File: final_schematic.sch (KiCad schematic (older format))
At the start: 50 parts, among them J1 Conn_Male, J2 Conn_Male, J3 Conn_01x04_Male, J4 Conn_01x02_Male, J5 Conn_Male, J6 Conn_Coaxial, J7 Conn_ARM_JTAG_SWD_10, J8 Conn_Male, SW1 SW_Push, SW2 SW_Push, SW3 SW_Push, U1 BNO055, U2 MTK3339, U3 STM32L476VGTx, U4 RFM95W-868S2, X1 SMA_EDGE_UFL

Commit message: pls no more
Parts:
- C11, C12, C13, C14, C15, C16: value 0.1 uF -> 0.1uF
- C6: value 100nF -> 0.1uF
- C7: value .12uF -> 0.12uF
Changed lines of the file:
@@
 P 2550 2250
 F 0 "C6" H 2665 2296 50  0000 L CNN
-F 1 "100nF" H 2665 2205 50  0000 L CNN
+F 1 "0.1uF" H 2665 2205 50  0000 L CNN
 F 2 "" H 2588 2100 50  0001 C CNN
 F 3 "~" H 2550 2250 50  0001 C CNN
@@
 AR Path="/5F8951F4" Ref="C11"  Part="1"
 F 0 "C11" H 4215 2096 50  0000 L CNN
-F 1 "0.1 uF" H 4215 2005 50  0000 L CNN
+F 1 "0.1uF" H 4215 2005 50  0000 L CNN
 F 2 "" H 4138 1900 50  0001 C CNN
 F 3 "~" H 4100 2050 50  0001 C CNN
@@
 AR Path="/5F8F3A53" Ref="C12"  Part="1"
 F 0 "C12" H 9665 5946 50  0000 L CNN
-F 1 "0.1 uF" H 9665 5855 50  0000 L CNN
+F 1 "0.1uF" H 9665 5855 50  0000 L CNN
 F 2 "" H 9588 5750 50  0001 C CNN
 F 3 "~" H 9550 5900 50  0001 C CNN
@@
 AR Path="/5F8F3A5A" Ref="C13"  Part="1"
 F 0 "C13" H 9915 5946 50  0000 L CNN
-F 1 "0.1 uF" H 9915 5855 50  0000 L CNN
+F 1 "0.1uF" H 9915 5855 50  0000 L CNN
 F 2 "" H 9838 5750 50  0001 C CNN
 F 3 "~" H 9800 5900 50  0001 C CNN
@@
 AR Path="/5F8F3A61" Ref="C14"  Part="1"
 F 0 "C14" H 10165 5946 50  0000 L CNN
-F 1 "0.1 uF" H 10165 5855 50  0000 L CNN
+F 1 "0.1uF" H 10165 5855 50  0000 L CNN
 F 2 "" H 10088 5750 50  0001 C CNN
 F 3 "~" H 10050 5900 50  0001 C CNN
@@
 AR Path="/5F8F3A68" Ref="C15"  Part="1"
 F 0 "C15" H 10415 5946 50  0000 L CNN
-F 1 "0.1 uF" H 10415 5855 50  0000 L CNN
+F 1 "0.1uF" H 10415 5855 50  0000 L CNN
 F 2 "" H 10338 5750 50  0001 C CNN
 F 3 "~" H 10300 5900 50  0001 C CNN
@@
 AR Path="/5F8F3A6F" Ref="C16"  Part="1"
 F 0 "C16" H 10665 5946 50  0000 L CNN
-F 1 "0.1 uF" H 10665 5855 50  0000 L CNN
+F 1 "0.1uF" H 10665 5855 50  0000 L CNN
 F 2 "" H 10588 5750 50  0001 C CNN
 F 3 "~" H 10550 5900 50  0001 C CNN
@@
 P 2850 1100
 F 0 "C7" H 2965 1146 50  0000 L CNN
-F 1 ".12uF" H 2965 1055 50  0000 L CNN
+F 1 "0.12uF" H 2965 1055 50  0000 L CNN
 F 2 "" H 2888 950 50  0001 C CNN
 F 3 "~" H 2850 1100 50  0001 C CNN

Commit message: Footprint Assignments Completed
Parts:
- C1, C11, C12, C5, C6: footprint (none) -> Capacitor_SMD:C_0402_1005Metric_Pad0.74x0.62mm_HandSolder
- C10, C2, C3, C4, C7, C8, C9: footprint (none) -> Capacitor_SMD:C_0603_1608Metric_Pad1.08x0.95mm_HandSolder
- C13: renamed from C18; footprint (none) -> Capacitor_SMD:C_0603_1608Metric_Pad1.08x0.95mm_HandSolder
- C14: renamed from C13; footprint (none) -> Capacitor_SMD:C_0402_1005Metric_Pad0.74x0.62mm_HandSolder
- C15: renamed from C14; footprint (none) -> Capacitor_SMD:C_0402_1005Metric_Pad0.74x0.62mm_HandSolder
- C16: renamed from C15; footprint (none) -> Capacitor_SMD:C_0402_1005Metric_Pad0.74x0.62mm_HandSolder
- C17: renamed from C16; footprint (none) -> Capacitor_SMD:C_0402_1005Metric_Pad0.74x0.62mm_HandSolder
- C18: renamed from C17; footprint (none) -> Capacitor_SMD:C_0402_1005Metric_Pad0.74x0.62mm_HandSolder
- D1: value LED -> LED_HEARTBEAT_R1; footprint (none) -> Diode_SMD:D_0603_1608Metric_Pad1.05x0.95mm_HandSolder
- D2: value LED -> LED_TRANSMIT_G1; footprint (none) -> Diode_SMD:D_0201_0603Metric_Pad0.64x0.40mm_HandSolder
- J1: footprint (none) -> Connector_PinHeader_1.00mm:PinHeader_1x06_P1.00mm_Vertical
- J2, J5: footprint (none) -> Connector_PinHeader_1.00mm:PinHeader_1x01_P1.00mm_Vertical
- J3: footprint (none) -> Connector_PinHeader_1.00mm:PinHeader_1x04_P1.00mm_Vertical
- J4: footprint (none) -> Connector_PinHeader_1.00mm:PinHeader_1x02_P1.00mm_Vertical
- J6, X1: footprint (none) -> Connector_Coaxial:U.FL_Molex_MCRF_73412-0110_Vertical
- J7: renamed from J8; footprint (none) -> Connector_PinHeader_1.00mm:PinHeader_1x01_P1.00mm_Vertical
- R1: footprint (none) -> Resistor_SMD:R_0402_1005Metric_Pad0.72x0.64mm_HandSolder
- R10, R2, R3, R4, R5, R6, R7, R8, R9, Re1, Rf1: footprint (none) -> Resistor_SMD:R_0603_1608Metric_Pad0.98x0.95mm_HandSolder
- RED1: value LED -> LED_GPS_R; footprint (none) -> Diode_SMD:D_0603_1608Metric_Pad1.05x0.95mm_HandSolder
- S1: footprint (none) -> Button_Switch_SMD:SW_DIP_SPSTx01_Slide_Omron_A6S-110x_W8.9mm_P2.54mm
- SW1: value SW_Push -> SW_Push_RST; footprint (none) -> Button_Switch_SMD:SW_SPST_PTS645
- SW2: value SW_Push -> SW_Push_RADIO; footprint (none) -> Button_Switch_SMD:SW_SPST_PTS645
- SW3: value SW_Push -> SW_Push_SESS; footprint (none) -> Button_Switch_SMD:SW_SPST_PTS645
- U2: footprint (none) -> footprint_lib:FGPMMOPA6H
- U4: footprint (none) -> RF_Module:HOPERF_RFM9XW_SMD
- renumbered J7 to J8

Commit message: Grouped Circuits/Re-arranged Schematic
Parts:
- removed C5: 0.1uF, Capacitor_SMD:C_0402_1005Metric_Pad0.74x0.62mm_HandSolder, symbol Device:C
- removed C7: 0.12uF, Capacitor_SMD:C_0603_1608Metric_Pad1.08x0.95mm_HandSolder, symbol Device:C
- removed C9: 0.0068uF, Capacitor_SMD:C_0603_1608Metric_Pad1.08x0.95mm_HandSolder, symbol Device:C
- added C?: 0.1uF, Capacitor_SMD:C_0402_1005Metric_Pad0.74x0.62mm_HandSolder, symbol Device:C
- added C?: 0.12uF, Capacitor_SMD:C_0603_1608Metric_Pad1.08x0.95mm_HandSolder, symbol Device:C
- added C?: 0.0068uF, Capacitor_SMD:C_0603_1608Metric_Pad1.08x0.95mm_HandSolder, symbol Device:C
- R1, Re1, Rf1: symbol Device:R -> Device:R_US
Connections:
- wire segments 243 -> 205
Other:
- note added: "Battery Babysitter \nConnector"
- note added: "GPS"
- note added: "IMU"
- note added: "OLED Breakout \nConnector"
- note added: "Power Switch"
- note added: "Power/Radio Transmit Indicator"
- note added: "STM32L4 Microcontroller"
- note removed: "Battery Babysitter Connector"
- note removed: "GPS\n"
- note removed: "IMU(BNO-005)"
- moved on the sheet: C1, C10, C11, C12, C13, C14, C15, C16, C17, C18, C2, C3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

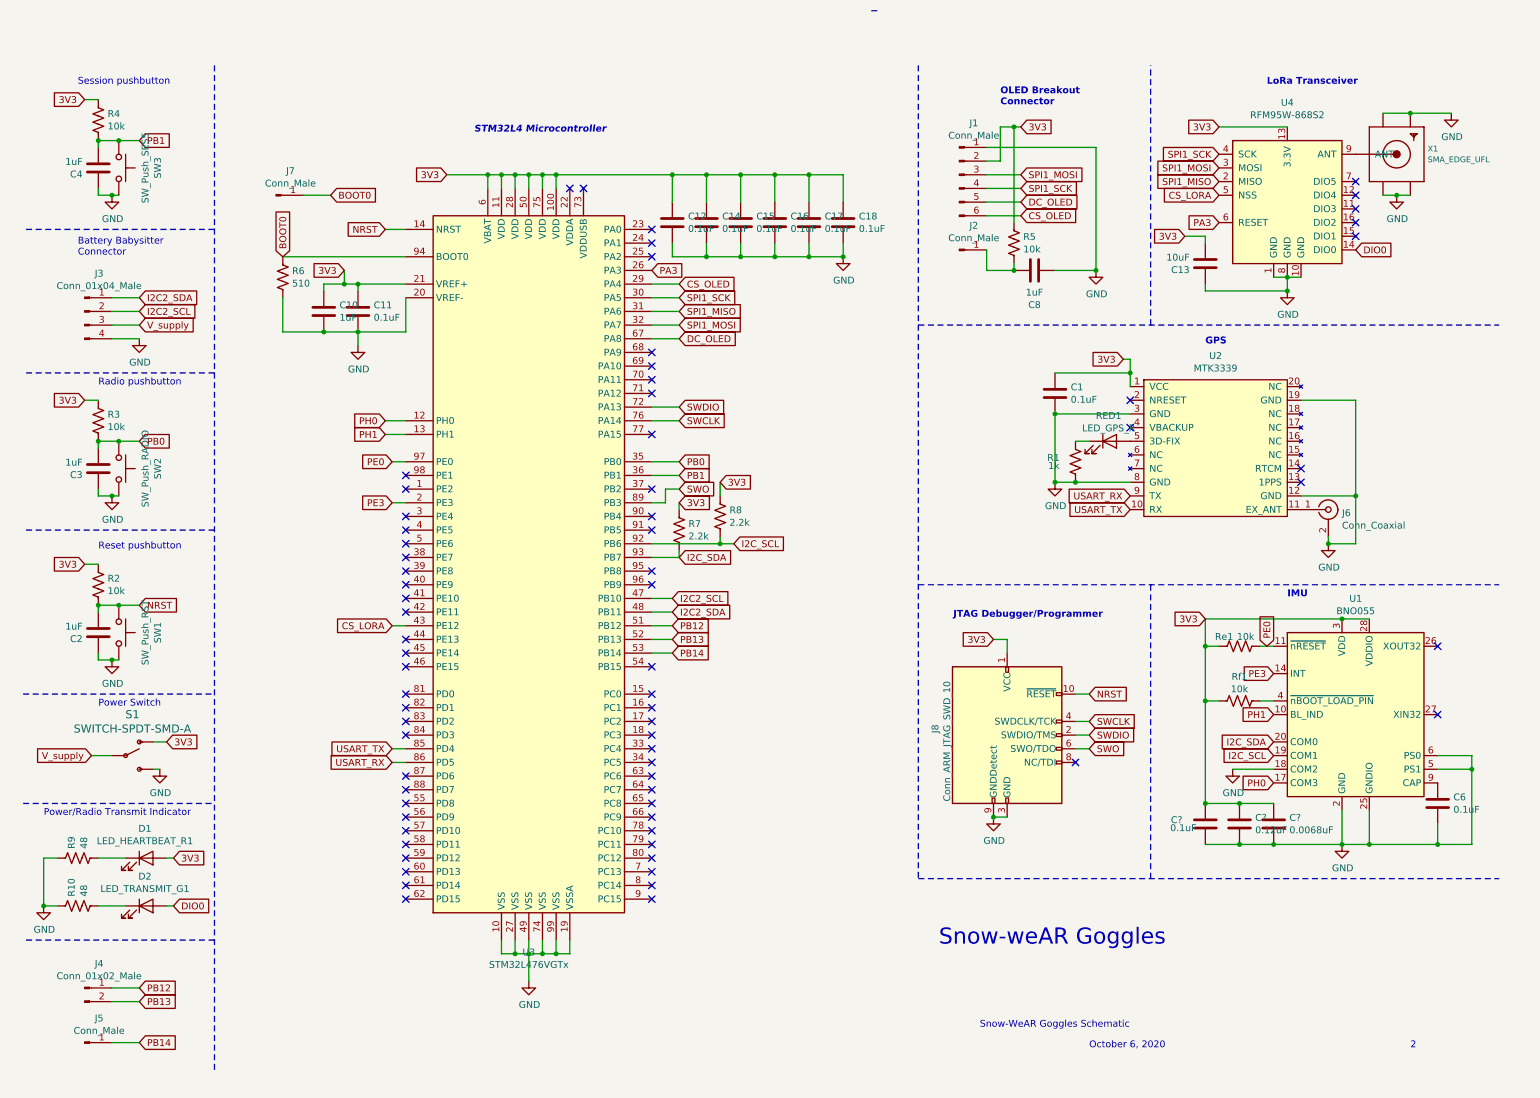
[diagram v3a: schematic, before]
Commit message: Updated Schematic from K improvements, also renamed
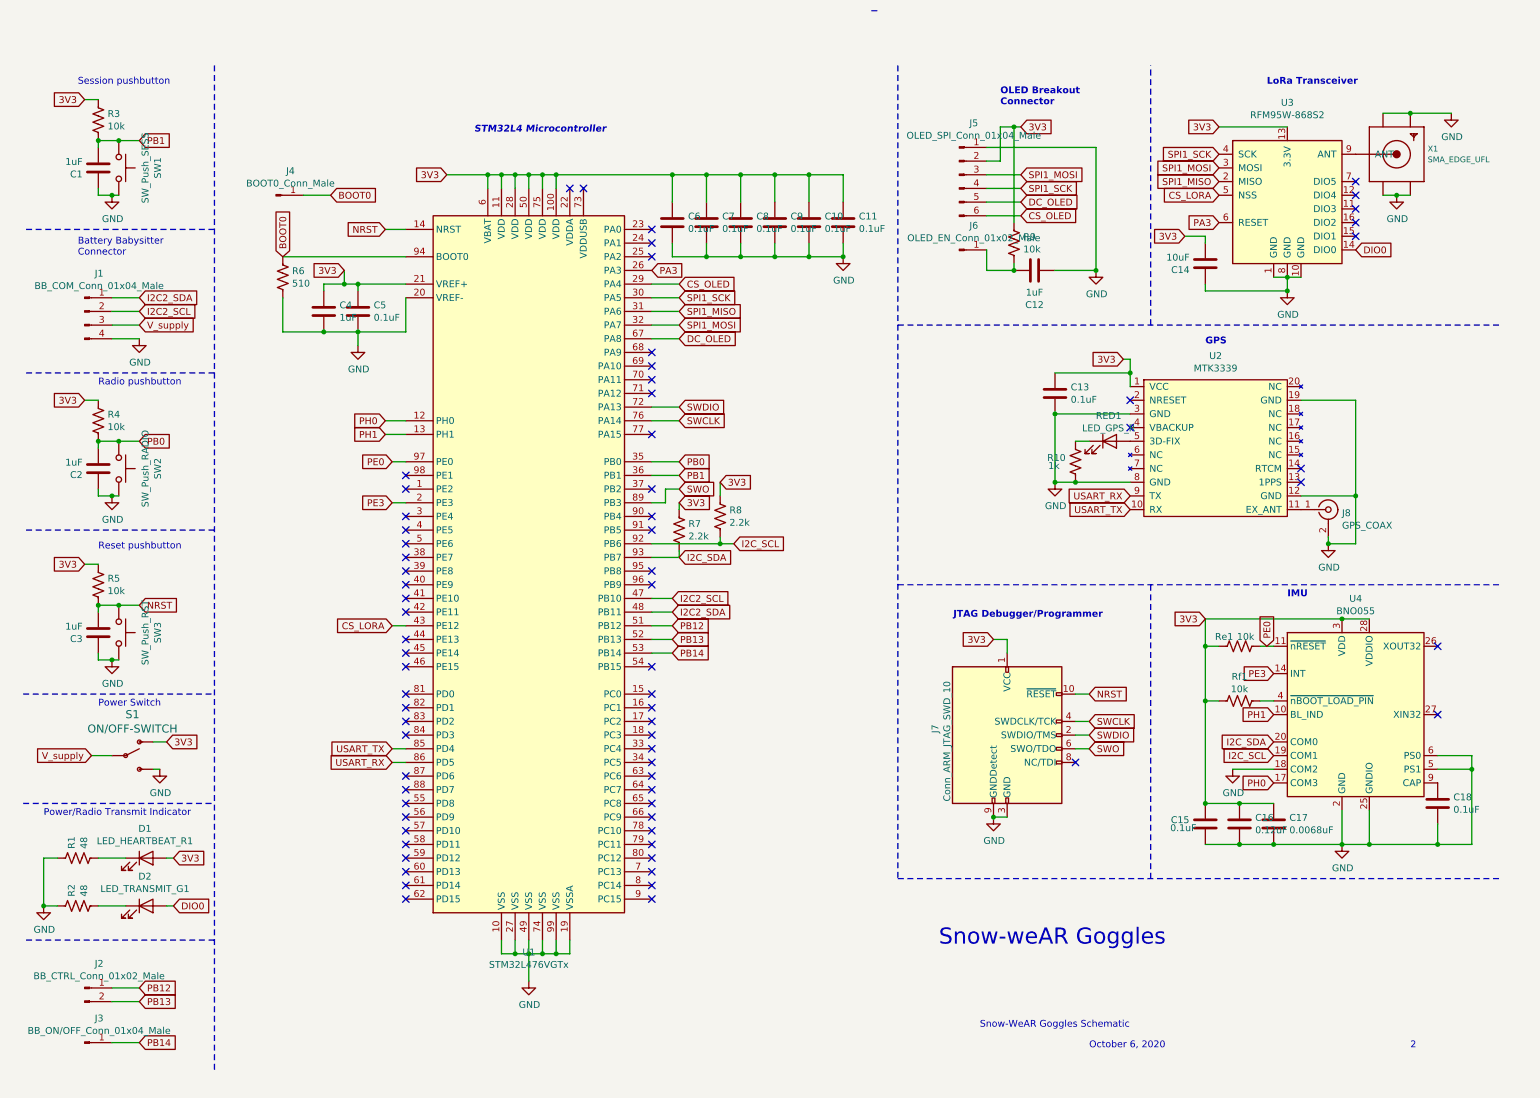
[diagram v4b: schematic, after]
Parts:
- J1: renamed from J3; value Conn_01x04_Male -> BB_COM_Conn_01x04_Male
- J2: renamed from J4; value Conn_01x02_Male -> BB_CTRL_Conn_01x02_Male
- J3: renamed from J5; value Conn_Male -> BB_ON/OFF_Conn_01x04_Male
- J4: renamed from J7; value Conn_Male -> BOOT0_Conn_Male
- J5: renamed from J1; value Conn_Male -> OLED_SPI_Conn_01x04_Male
- J6: renamed from J2; value Conn_Male -> OLED_EN_Conn_01x02_Male
- J8: renamed from J6; value Conn_Coaxial -> GPS_COAX
- S1: value SWITCH-SPDT-SMD-A -> ON/OFF-SWITCH
- gave numbers to parts that had none: 3
- renumbered C4 to C1, C17 to C10, C18 to C11, C8 to C12, C1 to C13, C13 to C14, C6 to C18, C3 to C2, C2 to C3, C10 to C4, C11 to C5, C12 to C6, C14 to C7, C15 to C8, C16 to C9, J8 to J7, R9 to R1, R1 to R10, R10 to R2, R4 to R3, R3 to R4, R2 to R5, R5 to R9, SW3 to SW1, SW1 to SW3, U3 to U1, U4 to U3, U1 to U4

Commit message: all footprints added to .kicad_pcb
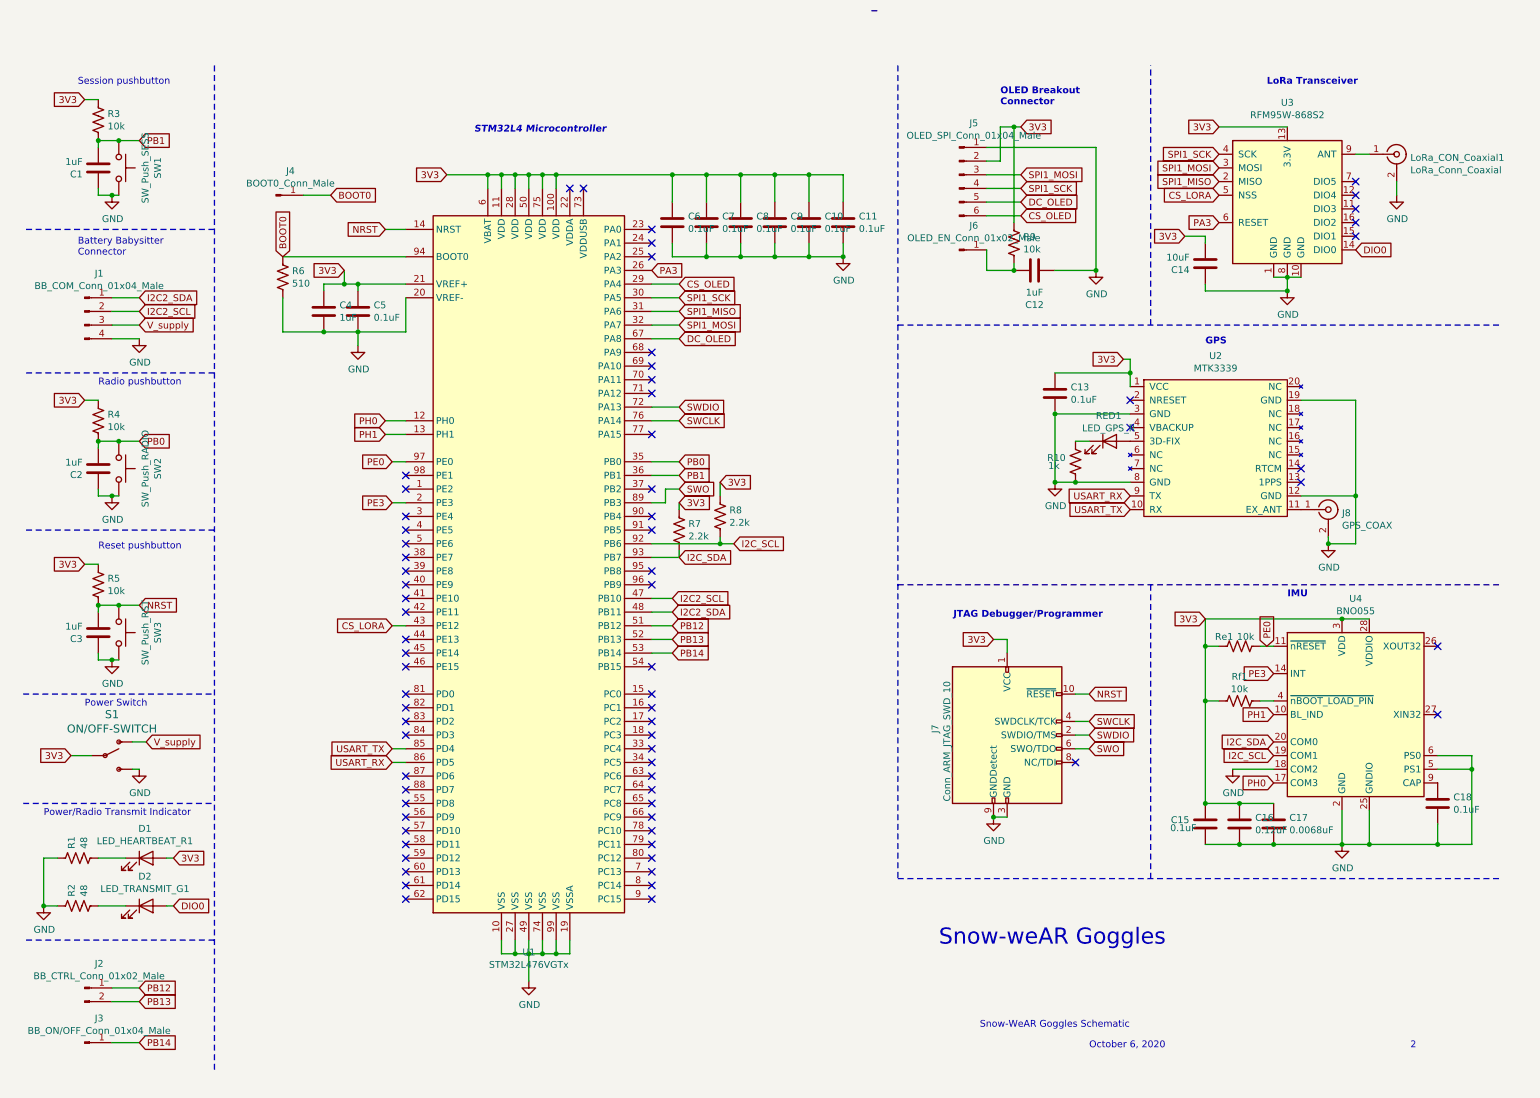
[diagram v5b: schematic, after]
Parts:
- removed X1: SMA_EDGE_UFL, Connector_Coaxial:U.FL_Molex_MCRF_73412-0110_Vertical, symbol final_schematic-eagle-import:SMACONNECTOR_EDGE_UFL
- added LoRa_CON_Coaxial1: LoRa_Conn_Coaxial, Connector_Coaxial:U.FL_Molex_MCRF_73412-0110_Vertical, symbol Connector:Conn_Coaxial
- S1: footprint Button_Switch_SMD:SW_DIP_SPSTx01_Slide_Omron_A6S-110x_W8.9mm_P2.54mm -> Button_Switch_SMD:SW_SP3T_PCM13
- SW1: footprint Button_Switch_SMD:SW_SPST_PTS645 -> Button_Switch_SMD:SW_SPDT_CK-JS102011SAQN
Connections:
- net 3V3: now also S1.2 (P); no longer S1.1 (O)
- net GND: now also LoRa_CON_Coaxial1.2 (Ext)
- net V_supply: now also S1.1 (O); no longer S1.2 (P)
- net at U3.9 (ANT): now also LoRa_CON_Coaxial1.1 (In)
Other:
- moved on the sheet: S1
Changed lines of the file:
@@
 Text GLabel 9200 1100 0    50   Input ~ 0
 SPI1_SCK
-$Comp
-L final_schematic-eagle-import:SMACONNECTOR_EDGE_UFL X1
-U 1 1 5F7841CC
-P 10500 1100
-F 0 "X1" H 10727 1140 42  0000 L CNN
-F 1 "SMA_EDGE_UFL" H 10727 1061 42  0000 L CNN
-F 2 "Connector_Coaxial:U.FL_Molex_MCRF_73412-0110_Vertical" H 10500 1100 50  0001 C CNN
-F 3 "" H 10500 1100 50  0001 C CNN
-	1    10500 1100
-	1    0    0    -1
-$EndComp
-Wire Wire Line
-	10400 1400 10500 1400
-$Comp
-L power:GND #PWR018
-U 1 1 5F7A7227
-P 10900 800
-F 0 "#PWR018" H 10900 550 50  0001 C CNN
-F 1 "GND" H 10905 627 50  0000 C CNN
-F 2 "" H 10900 800 50  0001 C CNN
-F 3 "" H 10900 800 50  0001 C CNN
-	1    10900 800
-	1    0    0    -1
-$EndComp
 Text GLabel 9200 1300 0    50   Input ~ 0
 SPI1_MISO
@@
 L final_schematic-rescue:SWITCH-SPDT-SMD-A-schematic-eagle-import S1
 U 1 1 60374331
-P 1200 5500
-F 0 "S1" H 1250 5801 59  0000 C CNN
-F 1 "ON/OFF-SWITCH" H 1250 5696 59  0000 C CNN
-F 2 "Button_Switch_SMD:SW_DIP_SPSTx01_Slide_Omron_A6S-110x_W8.9mm_P2.54mm" H 1200 5500 50  0001 C CNN
-F 3 "" H 1200 5500 50  0001 C CNN
-	1    1200 5500
+P 1050 5500
+F 0 "S1" H 1100 5801 59  0000 C CNN
+F 1 "ON/OFF-SWITCH" H 1100 5696 59  0000 C CNN
+F 2 "Button_Switch_SMD:SW_SP3T_PCM13" H 1050 5500 50  0001 C CNN
+F 3 "" H 1050 5500 50  0001 C CNN
+	1    1050 5500
 	1    0    0    -1
 $EndComp
@@
 L power:GND #PWR06
 U 1 1 6038CE54
-P 1450 5600
-F 0 "#PWR06" H 1450 5350 50  0001 C CNN
-F 1 "GND" H 1455 5427 50  0000 C CNN
-F 2 "" H 1450 5600 50  0001 C CNN
-F 3 "" H 1450 5600 50  0001 C CNN
-	1    1450 5600
-	1    0    0    -1
-$EndComp
-Text GLabel 950  5500 0    50   Input ~ 0
+P 1300 5600
+F 0 "#PWR06" H 1300 5350 50  0001 C CNN
+F 1 "GND" H 1305 5427 50  0000 C CNN
+F 2 "" H 1300 5600 50  0001 C CNN
+F 3 "" H 1300 5600 50  0001 C CNN
+	1    1300 5600
+	1    0    0    -1
+$EndComp
+Text GLabel 1350 5400 2    50   Input ~ 0
 V_supply
-Text GLabel 1500 5400 2    50   Input ~ 0
+Text GLabel 800  5500 0    50   Input ~ 0
 3V3
 Wire Wire Line
-	950  5500 1100 5500
-Wire Wire Line
-	1400 5400 1500 5400
-Wire Wire Line
-	1450 5600 1400 5600
+	800  5500 950  5500
+Wire Wire Line
+	1250 5400 1350 5400
+Wire Wire Line
+	1300 5600 1250 5600
 $Comp
 L Switch:SW_Push SW3
@@
 F 0 "SW1" H 1150 1485 50  0000 C CNN
 F 1 "SW_Push_SESS" H 1150 1394 50  0000 C CNN
-F 2 "Button_Switch_SMD:SW_SPST_PTS645" H 1150 1400 50  0001 C CNN
+F 2 "Button_Switch_SMD:SW_SPDT_CK-JS102011SAQN" H 1150 1400 50  0001 C CNN
 F 3 "" H 1150 1400 50  0001 C CNN
 	1    1150 1200
@@
 Wire Wire Line
 	7650 5950 7550 5950
-$Comp
-L power:GND #PWR017
-U 1 1 5F8112E2
-P 10500 1400
-F 0 "#PWR017" H 10500 1150 50  0001 C CNN
-F 1 "GND" H 10505 1227 50  0000 C CNN
-F 2 "" H 10500 1400 50  0001 C CNN
-F 3 "" H 10500 1400 50  0001 C CNN
-	1    10500 1400
-	1    0    0    -1
-$EndComp
 NoConn ~ 9800 3400
 NoConn ~ 9800 3500
@@
 	9100 2100 9700 2100
 Connection ~ 9700 2100
-Connection ~ 10500 1400
-Wire Wire Line
-	10500 1400 10600 1400
-Wire Wire Line
-	10400 800  10600 800
-Connection ~ 10600 800
-Wire Wire Line
-	10600 800  10900 800
 Wire Notes Line
 	8700 2350 8700 450
@@
 Text Notes 9100 2500 0    50   ~ 10
 GPS
-Text Notes 1000 5150 0    50   ~ 0
+Text Notes 900  5150 0    50   ~ 0
 Power Switch
 Wire Notes Line
@@
 Wire Notes Line
 	6850 6400 11250 6400
+$Comp
+L power:GND #PWR017
+U 1 1 5F8112E2
+P 10500 1400
+F 0 "#PWR017" H 10500 1150 50  0001 C CNN
+F 1 "GND" H 10505 1227 50  0000 C CNN
+F 2 "" H 10500 1400 50  0001 C CNN
+F 3 "" H 10500 1400 50  0001 C CNN
+	1    10500 1400
+	1    0    0    -1
+$EndComp
+Wire Wire Line
+	10200 1100 10300 1100
+Wire Wire Line
+	10500 1300 10500 1400
+$Comp
+L Connector:Conn_Coaxial LoRa_CON_Coaxial1
+U 1 1 5F8761EB
+P 10500 1100
+F 0 "LoRa_CON_Coaxial1" H 10600 1075 50  0000 L CNN
+F 1 "LoRa_Conn_Coaxial" H 10600 984 50  0000 L CNN
+F 2 "Connector_Coaxial:U.FL_Molex_MCRF_73412-0110_Vertical" H 10500 1100 50  0001 C CNN
+F 3 " ~" H 10500 1100 50  0001 C CNN
+	1    10500 1100
+	1    0    0    -1
+$EndComp
 $EndSCHEMATC

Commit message: BB Pin Updates and Flag Updates
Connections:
- net GND: now also J1.1 (Pin_1); no longer J1.4 (Pin_4)
- net I2C2_SCL: now also J1.4 (Pin_4); no longer J1.2 (Pin_2)
- net I2C2_SDA: now also J1.3 (Pin_3); no longer J1.1 (Pin_1)
- net V_supply: now also J1.2 (Pin_2); no longer J1.3 (Pin_3)
- net PA3 renamed LoRa_RST
- net PB0 renamed radio_btn
- net PB1 renamed session_btn
- net PB12 renamed BB_CE
- net PB13 renamed BB_GPOUT
- net PB14 renamed SYSOFF
- net PE0 renamed IMU_nRST
- net PE3 renamed IMU_INT
- net PH0 renamed IMU_COM3
- net PH1 renamed BL_IND
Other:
- moved on the sheet: D1, D2, J1, J2, J3, R1, R2
